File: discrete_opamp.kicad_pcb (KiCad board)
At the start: 2 copper layers, 38.1 x 20.3 mm, 25 parts, among them P1 PWR, P2 CONN_3, Q1 2SA1873, Q4 2SA1162S, Q5 2SC2712S, Q6 2SA1162S, Q7 FZT753CT, Q8 FZT653CT, Q9 2SA1162S

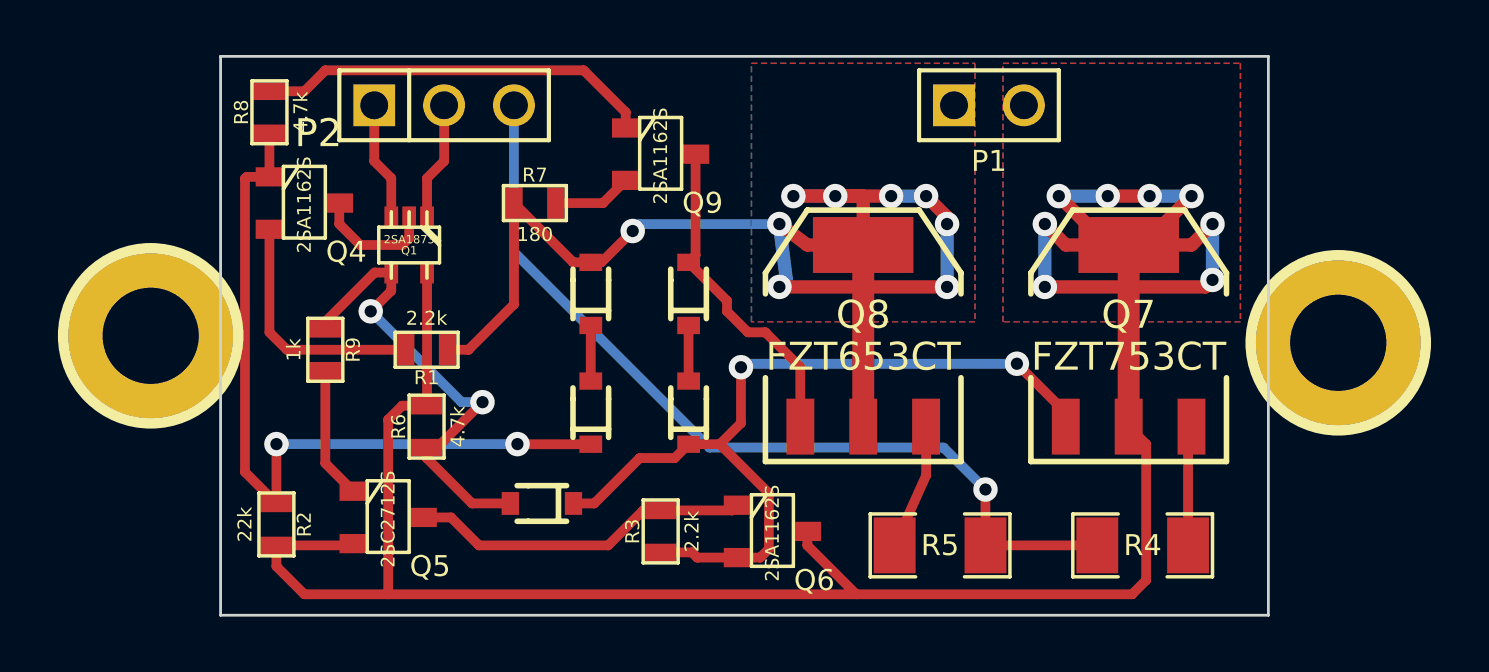
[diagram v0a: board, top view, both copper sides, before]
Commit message: Fixed border, added silkscreen text
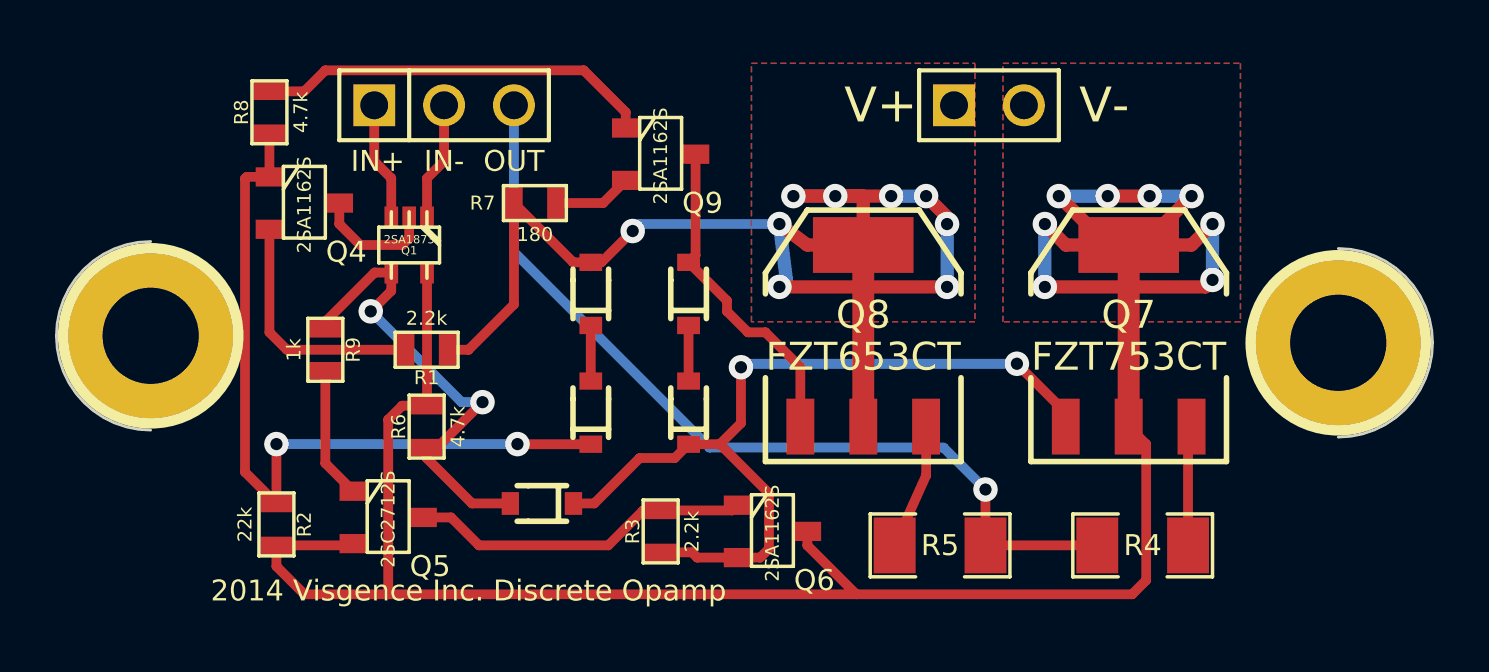
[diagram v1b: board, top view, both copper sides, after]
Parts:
- added G***: LOGO, LOGOMIRROR, B.Cu at (44.8, 36.2)
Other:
- board size 38.1 x 20.3 mm -> 50 x 7.1 mm
- board text added: "2014 Visgence Inc. Discrete Opamp"
- board text added: "IN+"
- board text added: "IN-"
- board text added: "OUT"
- board text added: "V+"
- board text added: "V-"
